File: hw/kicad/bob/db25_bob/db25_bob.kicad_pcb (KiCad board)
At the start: 2 copper layers, 98 x 72 mm, 83 parts, among them J1 DB25, J2 DB25, J3 RJ45, J4 RJ45, J5 RJ45, J6 RJ45, P1 DIL8, P2 DIL8, P3 DIL6, P4 DIL8, P5 DIL8, P6 DIL8, P7 DIL16, P8 DIL16, P9 DIL16, U1 ADuM1201WT, U10 ADuM1200CR, U11 ADuM1200CR, U12 ADuM1200CR, U13 ADuM1200CR, U14 ADuM1200CR, U2 ADuM1201WT, U3 ADuM1201WT, U4 ADuM1201WT, U5 ADuM1201WT, U6 ADuM1201WT, U7 ADuM1201WT, U8 ADuM1201WT, U9 ADuM1200CR

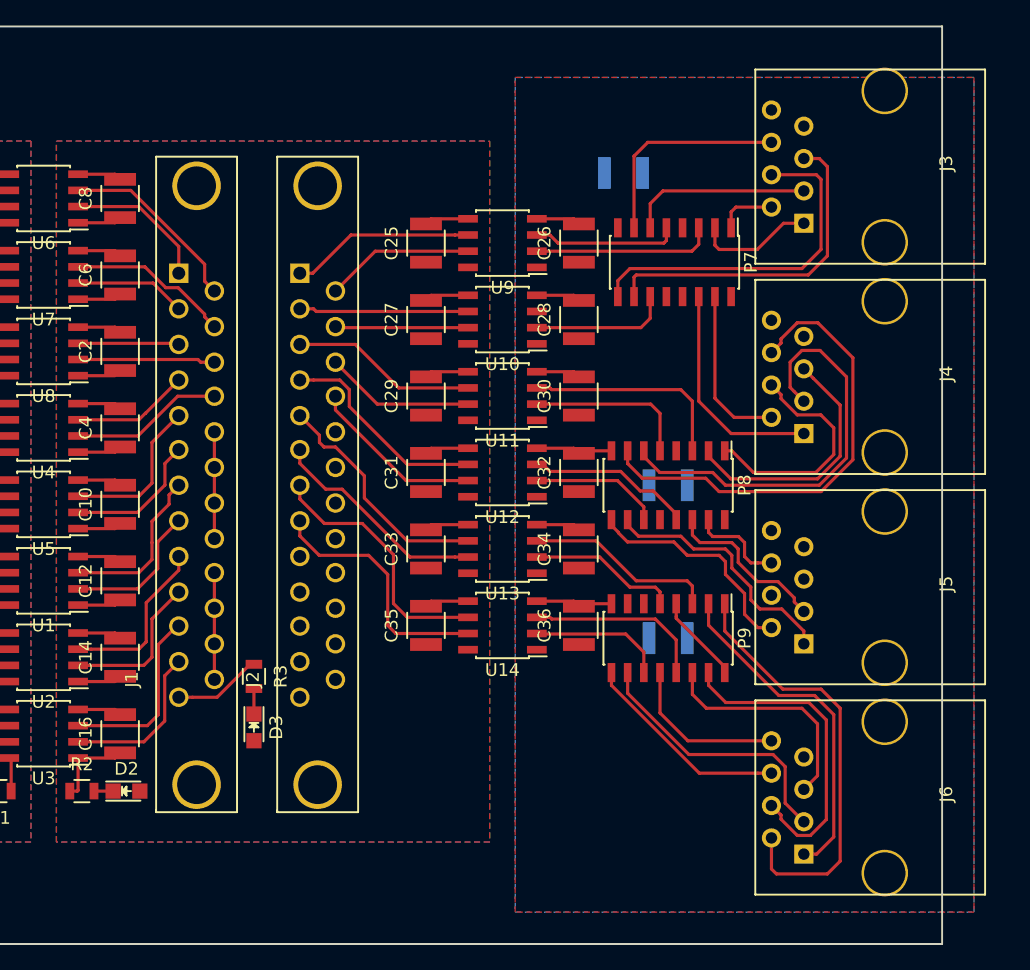
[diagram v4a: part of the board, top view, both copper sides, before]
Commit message: Finished routing the encoder side.
Power supply needs to be designed and SSerial side needs sockets.
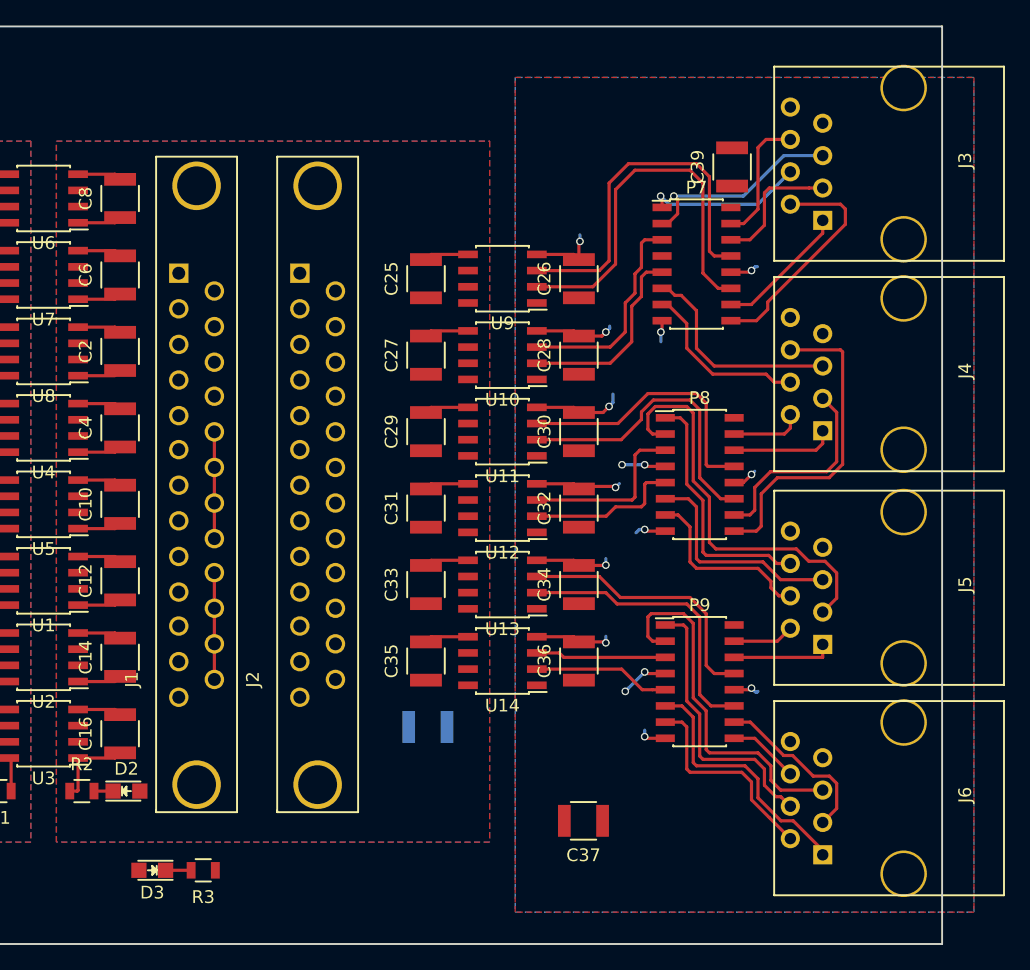
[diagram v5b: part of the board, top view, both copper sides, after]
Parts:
- C37, C39: moved to F.Cu
- moved C37 50.9 mm to (211.9, 132.3), turned to 180 degrees
- moved C39 37.3 mm to (223.5, 81.0), turned to 90 degrees
- moved C38 26.7 mm to (199.6, 125.0)
- moved R3 15.7 mm to (182.0, 136.2), turned to 180 degrees
- moved D3 13.8 mm to (178.0, 136.2), turned to 180 degrees
- moved P9 4.22 mm to (221.0, 121.4), turned to 0 degrees
- moved C25 2.79 mm to (199.5, 89.8)
- moved C26 2.79 mm to (211.5, 89.8)
- moved C27 2.79 mm to (199.5, 95.8)
- moved C28 2.79 mm to (211.5, 95.8)
- moved C29 2.79 mm to (199.5, 101.8)
- moved C30 2.79 mm to (211.5, 101.8)
- moved C31 2.79 mm to (199.5, 107.8)
- moved C32 2.79 mm to (211.5, 107.8)
- moved C33 2.79 mm to (199.5, 113.8)
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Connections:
- P7 pad 1: ENC0A- -> ENC0Z-
- P7 pad 10: ENC0Z+ -> ENC0A+
- P7 pad 11: ENC0Z -> ENC0A
- P7 pad 13: ENC1A -> ENC0B
- P7 pad 14: ENC1A+ -> ENC0B+
- P7 pad 15: ENC1A- -> ENC0B-
- P7 pad 2: ENC0A+ -> ENC0Z+
- P7 pad 3: ENC0A -> ENC0Z
- P7 pad 5: ENC0B -> ENC1Z
- P7 pad 6: ENC0B+ -> ENC1Z+
- P7 pad 7: ENC0B- -> ENC1Z-
- P7 pad 9: ENC0Z- -> ENC0A-
- P8 pad 1: ENC1Z- -> ENC2B-
- P8 pad 10: ENC2A+ -> ENC1B+
- P8 pad 11: ENC2A -> ENC1B
- P8 pad 13: ENC2B -> ENC1A
- P8 pad 14: ENC2B+ -> ENC1A+
- P8 pad 15: ENC2B- -> ENC1A-
- P8 pad 2: ENC1Z+ -> ENC2B+
- P8 pad 3: ENC1Z -> ENC2B
- P8 pad 5: ENC1B -> ENC2Z
- P8 pad 6: ENC1B+ -> ENC2Z+
- P8 pad 7: ENC1B- -> ENC2Z-
- P8 pad 9: ENC2A- -> ENC1B-
- P9 pad 1: ENC3A- -> ENC3Z-
- P9 pad 13: ENC3Z -> ENC2A
- P9 pad 14: ENC3Z+ -> ENC2A+
- P9 pad 15: ENC3Z- -> ENC2A-
- P9 pad 2: ENC3A+ -> ENC3Z+
- P9 pad 3: ENC3A -> ENC3Z
- P9 pad 5: ENC2Z -> ENC3A
- P9 pad 6: ENC2Z+ -> ENC3A+
- P9 pad 7: ENC2Z- -> ENC3A-
- U10 pad 2: ENC0Z -> ENC1Z
- U10 pad 3: ENC1A -> ENC0Z
- U10 pad 6: ENC1AO -> ENC0ZO
- U10 pad 7: ENC0ZO -> ENC1ZO
- U11 pad 3: ENC1Z -> ENC1A
- U11 pad 6: ENC1ZO -> ENC1AO
- U12 pad 2: ENC2A -> ENC2Z
- U12 pad 7: ENC2AO -> ENC2ZO
- U13 pad 2: ENC2Z -> ENC3B
- U13 pad 3: ENC3A -> ENC2A
- U13 pad 6: ENC3AO -> ENC2AO
- U13 pad 7: ENC2ZO -> ENC3BO
- U14 pad 2: ENC3B -> ENC3A
- U14 pad 7: ENC3BO -> ENC3AO
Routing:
- net ENC1A: track 0.00 -> 21.6 mm
- net ENC3ZO: track 20.4 -> 0.00 mm
- net ENC3BO: track 19.9 -> 0.00 mm
- net ENC2B+: track 13.2 -> 31.9 mm
- net ENC3AO: track 18.6 -> 0.00 mm
- net ENC3A-: track 34.1 -> 16.4 mm
- net ENC1B+: track 33.7 -> 16.2 mm
- net ENC2Z+: track 0.00 -> 17.4 mm
- net ENC2ZO: track 17.3 -> 0.00 mm
- net ENC0B: track 11.5 -> 28.7 mm
- net ENC2BO: track 16.7 -> 0.00 mm
- net ENC0A: track 14.2 -> 30.4 mm
- net ENC0Z-: track 27.8 -> 12.4 mm, vias 0 -> 1
- net IO1: track 14.7 -> 0.00 mm
- net ENC1ZO: track 14.6 -> 0.00 mm
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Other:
- net class Default: clearance 0.2 -> 0.22
- rule trace_clearance: 0.2 -> 0.22

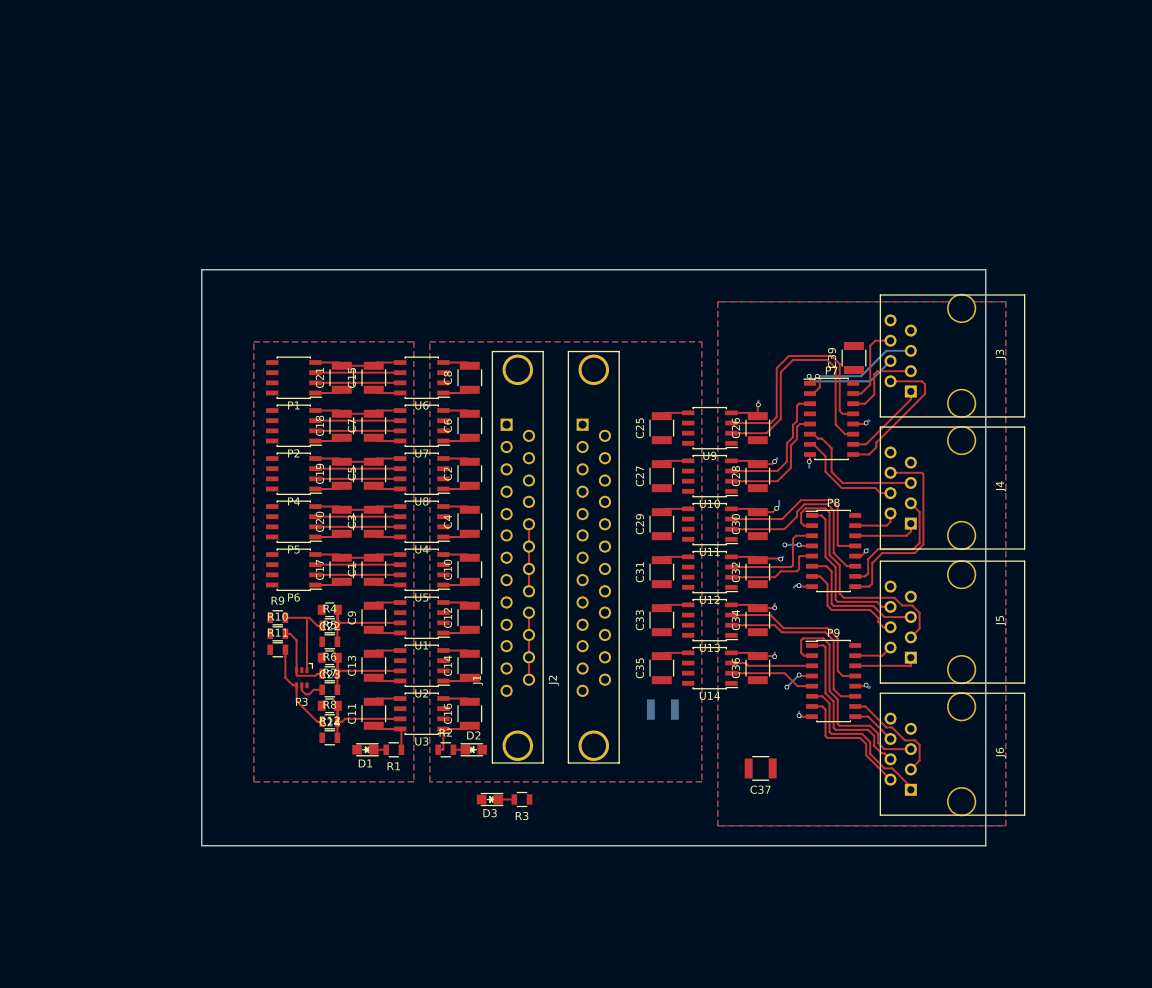
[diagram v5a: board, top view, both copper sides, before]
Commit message: Latest revision.
Still need to connect the rest of the IOs.
Increased PCB footprint to 100x100 to fit into Phoenix UM100 DIN Rail carriers.
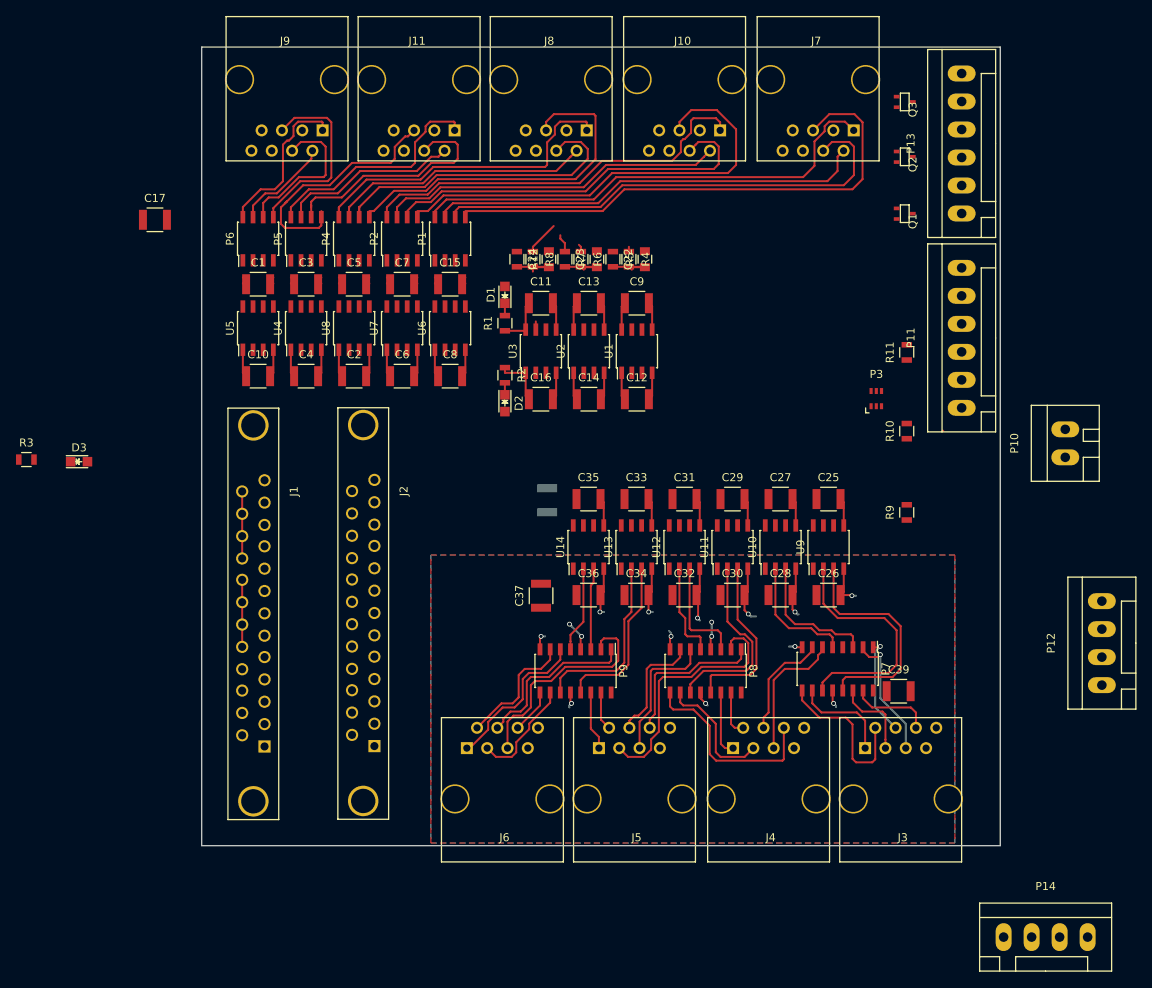
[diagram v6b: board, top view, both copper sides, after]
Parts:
- removed C18, C19, C20, C21: C, Capacitors_SMD:C_1210
- added J10: RJ45, Connect:RJ45_8, F.Cu at (202.3, 46.2)
- added J11: RJ45, Connect:RJ45_8, F.Cu at (169.2, 46.2)
- added J7: RJ45, Connect:RJ45_8, F.Cu at (219.0, 46.2)
- added J8: RJ45, Connect:RJ45_8, F.Cu at (185.7, 46.2)
- added J9: RJ45, Connect:RJ45_8, F.Cu at (152.7, 46.2)
- added P10: CONN_2, Sockets_WAGO734:WAGO_734_2pin_Straight_RuggedPads, F.Cu at (249.9, 91.7)
- added P11: CONN_6, Sockets_WAGO734:WAGO_734_6pin_Straight_RuggedPads, F.Cu at (237.0, 78.5)
- added P12: CONN_4, Sockets_WAGO734:WAGO_734_4pin_Straight_RuggedPads, F.Cu at (254.5, 116.7)
- added P13: CONN_6, Sockets_WAGO734:WAGO_734_6pin_Straight_RuggedPads, F.Cu at (237.0, 54.2)
- added P14: CONN_4, Sockets_WAGO734:WAGO_734_4pin_Straight_RuggedPads, F.Cu at (247.5, 153.4)
- added Q1: FET_N, Transistors_SMD:sc70, F.Cu at (229.9, 63.0)
- added Q2: FET_N, Transistors_SMD:sc70, F.Cu at (229.9, 55.9)
- added Q3: FET_N, Transistors_SMD:sc70, F.Cu at (229.9, 49.0)
- moved R11 87.0 mm to (230.1, 80.3), turned to 90 degrees
- moved R10 82.6 mm to (230.1, 90.2), turned to 90 degrees
- moved P3 79.8 mm to (226.3, 86.1), turned to 0 degrees
- moved R9 79.7 mm to (230.1, 100.3), turned to 90 degrees
- moved R3 75.1 mm to (120.1, 93.7), turned to 0 degrees
- moved D3 66.5 mm to (126.7, 94.0), turned to 0 degrees
- moved R12 64.2 mm to (181.4, 68.7), turned to 270 degrees
- moved R8 63.1 mm to (183.4, 68.7), turned to 270 degrees
- moved C24 62.2 mm to (185.4, 68.7), turned to 90 degrees
- moved R7 61.3 mm to (187.4, 68.7), turned to 270 degrees
- moved R6 60.6 mm to (189.4, 68.7), turned to 270 degrees
- moved C23 60.0 mm to (191.4, 68.7), turned to 90 degrees
- moved R5 59.5 mm to (193.4, 68.7), turned to 270 degrees
- moved D1 59.5 mm to (179.9, 73.1), turned to 90 degrees
- moved R4 59.1 mm to (195.4, 68.7), turned to 270 degrees
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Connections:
- C17 pad 1: +5VA -> +24V
- P1 pad 5: 0RX+ -> 0TX+
- P1 pad 6: 0RX- -> 0TX-
- P2 pad 5: 1RX+ -> 1TX+
- P2 pad 6: 1RX- -> 1TX-
- P4 pad 5: 2RX+ -> 2TX+
- P4 pad 6: 2RX- -> 2TX-
- P5 pad 5: 3RX+ -> 3TX+
- P5 pad 6: 3RX- -> 3TX-
- P6 pad 5: 4RX+ -> 4TX+
- P6 pad 6: 4RX- -> 4TX-
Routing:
- net 0TX+: track 0.00 -> 65.9 mm
- net 0TX-: track 0.00 -> 59.8 mm
- net 0RX+: track 0.00 -> 59.6 mm
- net 1TX+: track 0.00 -> 56.4 mm
- net 0RX-: track 0.00 -> 54.0 mm
- net 1RX+: track 0.00 -> 49.6 mm
- net EN-: track 116.0 -> 67.0 mm
- net 1TX-: track 0.00 -> 47.9 mm
- net 2TX+: track 0.00 -> 44.1 mm
- net 1RX-: track 0.00 -> 43.0 mm
- net 2RX+: track 0.00 -> 40.4 mm
- net 2TX-: track 0.00 -> 38.9 mm
- net 2RX-: track 0.00 -> 33.1 mm
- net 3TX+: track 0.00 -> 31.3 mm
- net +5VA: track 58.6 -> 28.4 mm
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- removed copper zone on F.Cu, net +5V
- removed copper zone on B.Cu, net GND
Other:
- board size 98 x 72 mm -> 99.8 x 99.8 mm

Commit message: routed some more.
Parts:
- moved R12 49.8 mm to (230.7, 75.4), turned to 0 degrees
- moved R8 47.5 mm to (230.7, 73.2), turned to 0 degrees
- moved R7 45.4 mm to (230.7, 82.3), turned to 0 degrees
- moved R6 42.8 mm to (230.7, 80.0), turned to 0 degrees
- moved R5 42.6 mm to (230.7, 89.2), turned to 0 degrees
- moved C24 42.0 mm to (226.8, 75.4), turned to 180 degrees
- moved D1 41.5 mm to (220.0, 62.3), turned to 0 degrees
- moved R4 39.7 mm to (230.6, 86.9), turned to 0 degrees
- moved R1 39.3 mm to (216.4, 62.3), turned to 0 degrees
- moved C23 38.0 mm to (226.8, 82.3), turned to 180 degrees
- moved R2 36.6 mm to (209.9, 62.3), turned to 180 degrees
- moved D2 36.1 mm to (206.4, 62.3), turned to 180 degrees
- moved C22 35.9 mm to (226.8, 89.2), turned to 180 degrees
- moved C11 35.3 mm to (218.9, 66.8), turned to 270 degrees
- moved U3 31.5 mm to (212.9, 66.8), turned to 0 degrees
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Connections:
- J1 pad 1: IO0 -> IO16
- J1 pad 10: IO13 -> IO6
- J1 pad 11: IO14 -> IO7
- J1 pad 12: IO15 -> IO8
- J1 pad 13: IO16 -> IO9
- J1 pad 14: IO1 -> IO10
- J1 pad 15: IO3 -> IO12
- J1 pad 16: IO5 -> IO14
- J1 pad 17: IO7 -> IO0
- J1 pad 2: IO2 -> IO11
- J1 pad 3: IO4 -> IO13
- J1 pad 4: IO6 -> IO15
- J1 pad 5: IO8 -> IO1
- J1 pad 6: IO9 -> IO2
- J1 pad 7: IO10 -> IO3
- J1 pad 8: IO11 -> IO4
- J1 pad 9: IO12 -> IO5
- J2 pad 1: ENC0BO -> Net-(J2-Pad1)
- J2 pad 10: Net-(J2-Pad10) -> ENC1ZO
- J2 pad 11: Net-(J2-Pad11) -> ENC0ZO
- J2 pad 12: Net-(J2-Pad12) -> ENC0AO
- J2 pad 13: Net-(J2-Pad13) -> ENC0BO
- J2 pad 14: ENC0AO -> Net-(J2-Pad14)
- J2 pad 15: ENC0ZO -> Net-(J2-Pad15)
- J2 pad 16: ENC1BO -> ENC3AO
- J2 pad 17: ENC2AO -> ENC3BO
- J2 pad 2: ENC1AO -> Net-(J2-Pad2)
- J2 pad 3: ENC1ZO -> Net-(J2-Pad3)
- J2 pad 4: ENC2BO -> ENC3ZO
- J2 pad 5: ENC3AO -> ENC2AO
- J2 pad 7: ENC3ZO -> ENC2BO
- J2 pad 8: ENC3BO -> ENC1BO
- J2 pad 9: Net-(J2-Pad9) -> ENC1AO
- U1 pad 6: OUT0 -> IN0P
- U1 pad 7: IN0P -> OUT0
- U2 pad 6: OUT1 -> IN1P
- U2 pad 7: IN1P -> OUT1
- U3 pad 6: OUT2 -> IN2P
- U3 pad 7: IN2P -> OUT2
- U6 pad 2: IO0 -> IO1
- U6 pad 3: IO1 -> IO0
- U7 pad 2: IO2 -> IO3
- U7 pad 3: IO3 -> IO2
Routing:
- net IO14: track 0.15 -> 108.4 mm
- net IO12: track 0.00 -> 106.1 mm
- net IO15: track 0.00 -> 105.7 mm
- net IO10: track 0.47 -> 102.8 mm
- net IO13: track 0.00 -> 102.3 mm
- net IO11: track 0.00 -> 99.6 mm
- net ENC0BO: track 0.00 -> 67.5 mm
- net ENC0AO: track 0.00 -> 67.5 mm
- net ENC1ZO: track 0.00 -> 65.0 mm
- net ENC0ZO: track 0.00 -> 64.4 mm
- net ENC1BO: track 0.00 -> 64.1 mm
- net ENC1AO: track 0.00 -> 63.1 mm
- net ENC2ZO: track 0.00 -> 61.6 mm
- net ENC2BO: track 0.00 -> 60.9 mm
- net ENC3BO: track 0.00 -> 60.5 mm
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- added copper zone on F.Cu, net +5V
